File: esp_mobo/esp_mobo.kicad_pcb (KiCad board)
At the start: 2 copper layers, 75.5 x 107 mm, 4 parts, among them J1 JST XH Power in, U1 ESP32-DevKitC, U2 74AHCT125

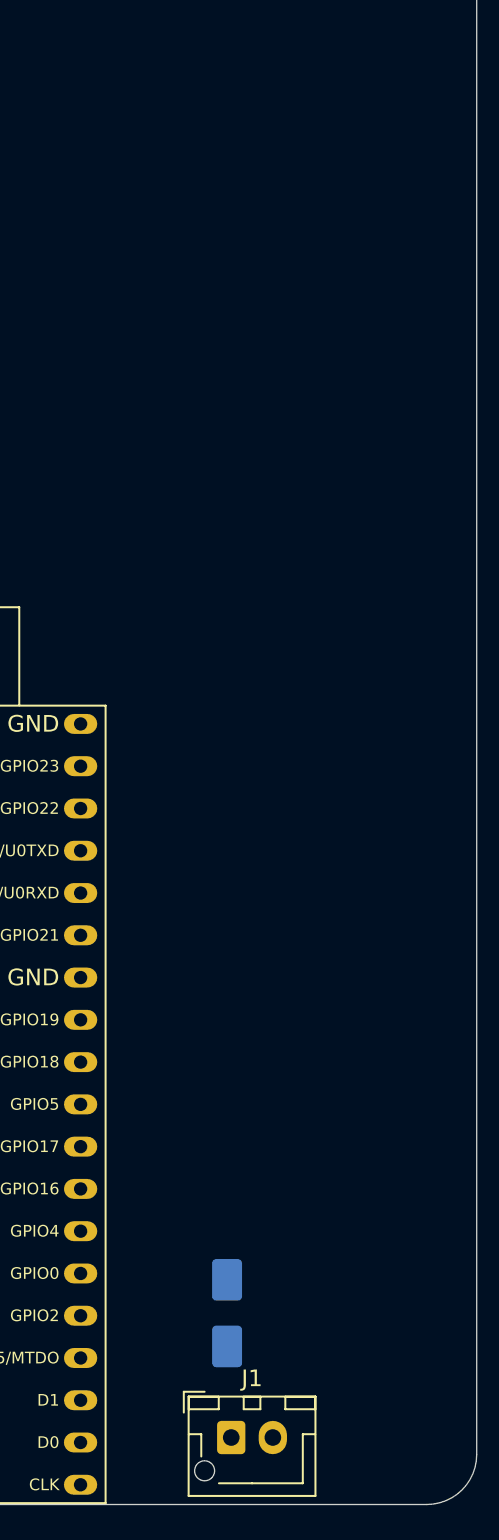
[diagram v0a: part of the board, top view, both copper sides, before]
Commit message: add submodule for testing
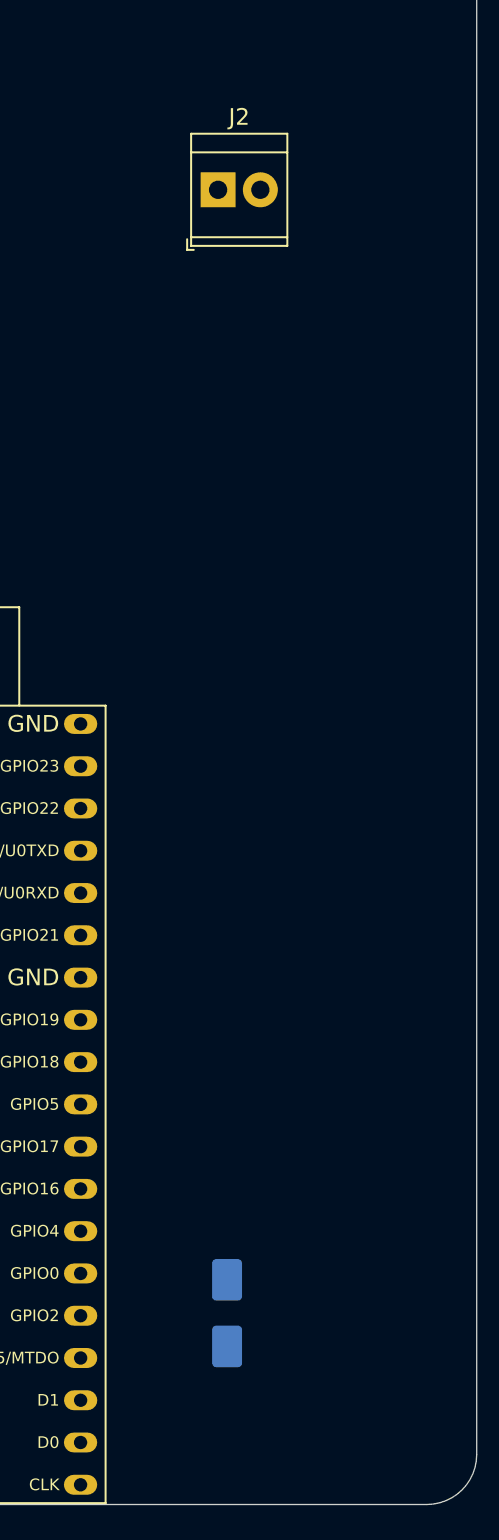
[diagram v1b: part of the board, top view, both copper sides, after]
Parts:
- removed J1: JST XH Power in, Connector_JST:JST_XH_B2B-XH-AM_1x02_P2.50mm_Vertical
- added J2: Screw_Terminal_01x02, TerminalBlock_TE-Connectivity:TerminalBlock_TE_282834-2_1x02_P2.54mm_Horizontal, F.Cu at (168.0, 62.5)
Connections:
- U1 pad 12: unconnected-(U1-MTMS/GPIO14/ADC2_CH6-Pad12) -> Motor 3 Signal
- U1 pad 13: unconnected-(U1-MTDI/GPIO12/ADC2_CH5-Pad13) -> Motor 1 Signal
- U1 pad 15: unconnected-(U1-MTCK/GPIO13/ADC2_CH4-Pad15) -> Motor 2 Signal
- U1 pad 23: unconnected-(U1-MTDO/GPIO15/ADC2_CH3-Pad23) -> Motor 4 Signal
- U1 pad 24: unconnected-(U1-ADC2_CH2/GPIO2-Pad24) -> Neopixel Data Out 3.3V
- U1 pad 27: unconnected-(U1-GPIO16-Pad27) -> Motor 5 Signal
- U1 pad 28: unconnected-(U1-GPIO17-Pad28) -> Motor 6 Signal
- U1 pad 30: unconnected-(U1-GPIO18-Pad30) -> Motor 7 Signal
- U1 pad 31: unconnected-(U1-GPIO19-Pad31) -> Motor 8 Signal
- U1 pad 34: unconnected-(U1-U0RXD/GPIO3-Pad34) -> RX
- U1 pad 35: unconnected-(U1-U0TXD/GPIO1-Pad35) -> TX
- U2 pad 1: unconnected-(U2-Pad1) -> GND
- U2 pad 10: unconnected-(U2-Pad10) -> GND
- U2 pad 13: unconnected-(U2-Pad13) -> GND
- U2 pad 14: unconnected-(U2E-VCC-Pad14) -> +5V
- U2 pad 2: unconnected-(U2-Pad2) -> Neopixel Data Out 3.3V
- U2 pad 3: unconnected-(U2-Pad3) -> Neopixel Data Out 5V
- U2 pad 4: unconnected-(U2-Pad4) -> GND
- U2 pad 7: unconnected-(U2E-GND-Pad7) -> GND

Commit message: Update ESC Mobo
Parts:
- added 5V: Conn_01x03_Pin, Connector_PinHeader_2.54mm:PinHeader_1x03_P2.54mm_Vertical, F.Cu at (115.1, 54.1)
- added F1: Polyfuse, Fuse:Fuse_Bourns_MF-RG300, F.Cu at (126.4, 56.5)
- added GND: Conn_01x03_Pin, Connector_PinHeader_2.54mm:PinHeader_1x03_P2.54mm_Vertical, F.Cu at (110.0, 54.1)
- added J1: Conn_01x04_Pin, Connector_JST:JST_XH_B4B-XH-AM_1x04_P2.50mm_Vertical, F.Cu at (152.9, 38.5)
- added J3: Conn_01x03_Pin, Connector_JST:JST_XH_B3B-XH-AM_1x03_P2.50mm_Vertical, F.Cu at (127.4, 38.5)
- added J4: Conn_01x03_Pin, Connector_JST:JST_XH_B3B-XH-AM_1x03_P2.50mm_Vertical, F.Cu at (138.9, 38.5)
- added R1: 220, Resistor_SMD:R_0805_2012Metric_Pad1.20x1.40mm_HandSolder, F.Cu at (125.0, 46.0)
- added R10: 220, Resistor_SMD:R_0603_1608Metric_Pad0.98x0.95mm_HandSolder, F.Cu at (144.8, 53.0)
- added R11: 220, Resistor_SMD:R_0603_1608Metric_Pad0.98x0.95mm_HandSolder, F.Cu at (144.8, 55.5)
- added R12: 220, Resistor_SMD:R_0603_1608Metric_Pad0.98x0.95mm_HandSolder, F.Cu at (116.5, 77.5)
- added R13: 220, Resistor_SMD:R_0603_1608Metric_Pad0.98x0.95mm_HandSolder, F.Cu at (116.5, 82.5)
- added R14: 220, Resistor_SMD:R_0603_1608Metric_Pad0.98x0.95mm_HandSolder, F.Cu at (149.2, 48.0)
- added R15: 220, Resistor_SMD:R_0603_1608Metric_Pad0.98x0.95mm_HandSolder, F.Cu at (149.2, 50.5)
- added R16: 220, Resistor_SMD:R_0603_1608Metric_Pad0.98x0.95mm_HandSolder, F.Cu at (149.2, 53.0)
- added R17: 220, Resistor_SMD:R_0603_1608Metric_Pad0.98x0.95mm_HandSolder, F.Cu at (149.2, 55.5)
- added R2: 220, Resistor_SMD:R_0603_1608Metric_Pad0.98x0.95mm_HandSolder, F.Cu at (140.5, 48.0)
- added R3: 220, Resistor_SMD:R_0603_1608Metric_Pad0.98x0.95mm_HandSolder, F.Cu at (140.5, 50.5)
- added R4: 220, Resistor_SMD:R_0603_1608Metric_Pad0.98x0.95mm_HandSolder, F.Cu at (159.0, 77.0)
- added R5: 220, Resistor_SMD:R_0603_1608Metric_Pad0.98x0.95mm_HandSolder, F.Cu at (159.0, 82.5)
- added R6: 220, Resistor_SMD:R_0603_1608Metric_Pad0.98x0.95mm_HandSolder, F.Cu at (175.0, 67.0)
- added R7: 220, Resistor_SMD:R_0603_1608Metric_Pad0.98x0.95mm_HandSolder, F.Cu at (175.0, 72.5)
- added R8: 220, Resistor_SMD:R_0603_1608Metric_Pad0.98x0.95mm_HandSolder, F.Cu at (144.8, 48.0)
- added R9: 220, Resistor_SMD:R_0603_1608Metric_Pad0.98x0.95mm_HandSolder, F.Cu at (144.8, 50.5)
- added Sig: Conn_01x03_Pin, Connector_PinHeader_2.54mm:PinHeader_1x03_P2.54mm_Vertical, F.Cu at (112.5, 54.1)
- added U3: PC847, Package_DIP:DIP-16_W7.62mm, F.Cu at (163.3, 67.1)
- added U4: PC847, Package_DIP:DIP-16_W7.62mm, F.Cu at (120.6, 67.1)
- D1: moved to F.Cu
- moved D1 82.6 mm to (172.0, 47.5)
- moved U2 48.0 mm to (141.9, 67.1)
- moved J2 24.0 mm to (169.2, 38.5)
- moved U1 1.25 mm to (133.1, 94.6)
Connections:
- D1 pad 2: Net-(D1-A) -> GND
- J2 pad 1: Net-(D1-A) -> Net-(J2-Pin_1)
- U1 pad 26: unconnected-(U1-ADC2_CH0/GPIO4-Pad26) -> Servo1 Data In
- U1 pad 7: unconnected-(U1-32K_XP/GPIO32/ADC1_CH4-Pad7) -> Servo2 Data In
- U1 pad 8: unconnected-(U1-32K_XN/GPIO33/ADC1_CH5-Pad8) -> Servo3 Data In
- U2 pad 11: unconnected-(U2-Pad11) -> Servo3 Data Out
- U2 pad 12: unconnected-(U2-Pad12) -> Servo3 Data In
- U2 pad 5: unconnected-(U2-Pad5) -> Servo1 Data In
- U2 pad 6: unconnected-(U2-Pad6) -> Servo1 Data Out
- U2 pad 8: unconnected-(U2-Pad8) -> Servo2 Data Out
- U2 pad 9: unconnected-(U2-Pad9) -> Servo2 Data In

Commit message: Update ESC Mobo
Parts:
- removed 5V, GND, Sig: Conn_01x03_Pin, Connector_PinHeader_2.54mm:PinHeader_1x03_P2.54mm_Vertical
- added C1: C_Polarized, Capacitor_THT:CP_Radial_D5.0mm_P2.00mm, F.Cu at (169.5, 55.0)
- added C2: 100uf, Capacitor_SMD:C_0603_1608Metric, F.Cu at (137.5, 51.5)
- added C3: 100uf, Capacitor_SMD:C_0603_1608Metric, F.Cu at (157.0, 51.5)
- added C4: 100uf, Capacitor_SMD:C_0603_1608Metric, F.Cu at (150.5, 51.5)
- added C5: 100uf, Capacitor_SMD:C_0603_1608Metric, F.Cu at (144.0, 51.5)
- added D2: WS2812B, LED_SMD:LED_WS2812B_PLCC4_5.0x5.0mm_P3.2mm, F.Cu at (134.8, 57.0)
- added D3: WS2812B, LED_SMD:LED_WS2812B_PLCC4_5.0x5.0mm_P3.2mm, F.Cu at (141.4, 57.0)
- added D4: WS2812B, LED_SMD:LED_WS2812B_PLCC4_5.0x5.0mm_P3.2mm, F.Cu at (148.0, 57.0)
- added D5: WS2812B, LED_SMD:LED_WS2812B_PLCC4_5.0x5.0mm_P3.2mm, F.Cu at (154.6, 57.0)
- added H1: MountingHole_Pad, MountingHole:MountingHole_3.2mm_M3_Pad, F.Cu at (178.0, 40.0)
- added H2: MountingHole_Pad, MountingHole:MountingHole_3.2mm_M3_Pad, F.Cu at (113.5, 40.0)
- added H3: MountingHole_Pad, MountingHole:MountingHole_3.2mm_M3_Pad, F.Cu at (113.5, 136.0)
- added H4: MountingHole_Pad, MountingHole:MountingHole_3.2mm_M3_Pad, F.Cu at (178.0, 136.0)
- added J10: Conn_01x03_Pin, Connector_PinHeader_2.54mm:PinHeader_1x03_P2.54mm_Vertical, F.Cu at (178.6, 101.5)
- added J11: Conn_01x03_Pin, Connector_PinHeader_2.54mm:PinHeader_1x03_P2.54mm_Vertical, F.Cu at (178.6, 105.0)
- added J12: Conn_01x03_Pin, Connector_PinHeader_2.54mm:PinHeader_1x03_P2.54mm_Vertical, F.Cu at (178.6, 108.5)
- added J13: Conn_01x03_Pin, Connector_PinHeader_2.54mm:PinHeader_1x03_P2.54mm_Vertical, F.Cu at (178.6, 115.0)
- added J14: Conn_01x03_Pin, Connector_PinHeader_2.54mm:PinHeader_1x03_P2.54mm_Vertical, F.Cu at (178.6, 122.8)
- added J15: Conn_01x03_Pin, Connector_PinHeader_2.54mm:PinHeader_1x03_P2.54mm_Vertical, F.Cu at (178.6, 112.0)
- added J16: Conn_01x02_Pin, Connector_PinHeader_2.54mm:PinHeader_1x02_P2.54mm_Vertical, F.Cu at (168.5, 110.0)
- added J5: Conn_01x03_Pin, Connector_PinHeader_2.54mm:PinHeader_1x03_P2.54mm_Vertical, F.Cu at (111.5, 51.5)
- added J6: Conn_01x03_Pin, Connector_PinHeader_2.54mm:PinHeader_1x03_P2.54mm_Vertical, F.Cu at (114.0, 51.5)
- added J7: Conn_01x03_Pin, Connector_PinHeader_2.54mm:PinHeader_1x03_P2.54mm_Vertical, F.Cu at (116.6, 51.5)
- added J8: Conn_01x03_Pin, Connector_PinHeader_2.54mm:PinHeader_1x03_P2.54mm_Vertical, F.Cu at (178.6, 95.0)
- added J9: Conn_01x03_Pin, Connector_PinHeader_2.54mm:PinHeader_1x03_P2.54mm_Vertical, F.Cu at (178.6, 98.0)
- moved R9 44.0 mm to (175.0, 82.5)
- moved F1 42.7 mm to (167.5, 45.0), turned to -90 degrees
- moved R8 41.9 mm to (175.0, 77.0)
- moved R11 32.6 mm to (117.0, 72.5)
- moved R17 31.8 mm to (132.5, 82.5), turned to 180 degrees
- moved R10 31.2 mm to (117.0, 67.0)
- moved R16 29.3 mm to (132.5, 77.0), turned to 180 degrees
- moved R3 29.1 mm to (160.0, 72.0)
- moved R2 27.3 mm to (160.0, 67.0)
- moved R15 27.3 mm to (132.5, 72.0), turned to 180 degrees
- moved R14 25.3 mm to (132.5, 67.0), turned to 180 degrees
- moved D1 2.00 mm to (174.0, 47.5), turned to 90 degrees
- moved R1 1.00 mm to (125.0, 45.0)
- moved R4 1.00 mm to (160.0, 77.0)
- moved R5 1.00 mm to (160.0, 82.5)
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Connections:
- U2 pad 3: Neopixel Data Out 5V -> NeoPixel Onboard
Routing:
- net GND: track 0.00 -> 166.8 mm, vias 0 -> 1
- net Motor 2 Signal: track 0.00 -> 115.1 mm
- net Motor 7 Signal: track 0.00 -> 109.5 mm
- net Motor 3 Signal: track 0.00 -> 109.4 mm
- net Motor 1 Signal: track 0.00 -> 106.4 mm
- net Motor 8 Signal: track 0.00 -> 94.9 mm
- net +5V: track 0.00 -> 91.9 mm
- net Neopixel Data Out 3.3V: track 0.00 -> 83.1 mm
- net Servo1 Data In: track 0.00 -> 76.8 mm
- net SDA: track 0.00 -> 72.1 mm
- net SCL: track 0.00 -> 69.1 mm
- net Motor 4 Signal: track 0.00 -> 63.0 mm
- net Servo2 Data Out: track 0.00 -> 57.4 mm, vias 0 -> 1
- net Servo1 Data Out: track 0.00 -> 54.9 mm
- net NeoPixel Onboard: track 0.00 -> 53.4 mm
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- added copper zone on F.Cu, net +5V
- added copper zone on B.Cu, net GND

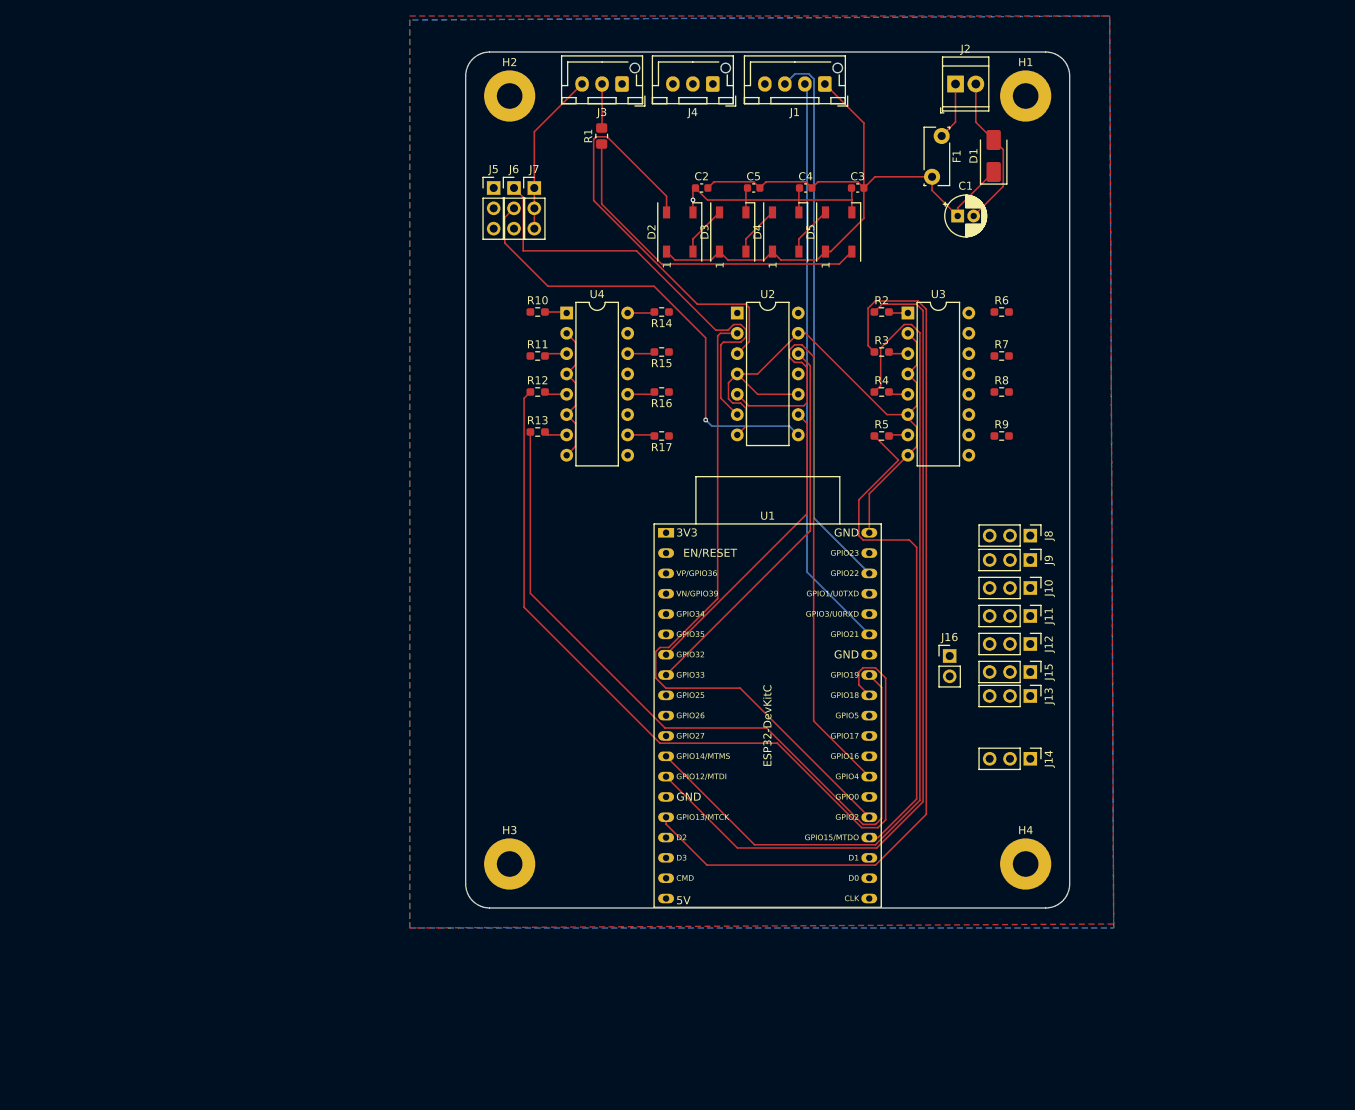
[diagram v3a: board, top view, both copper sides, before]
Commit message: Update ESC Mobo with BME280
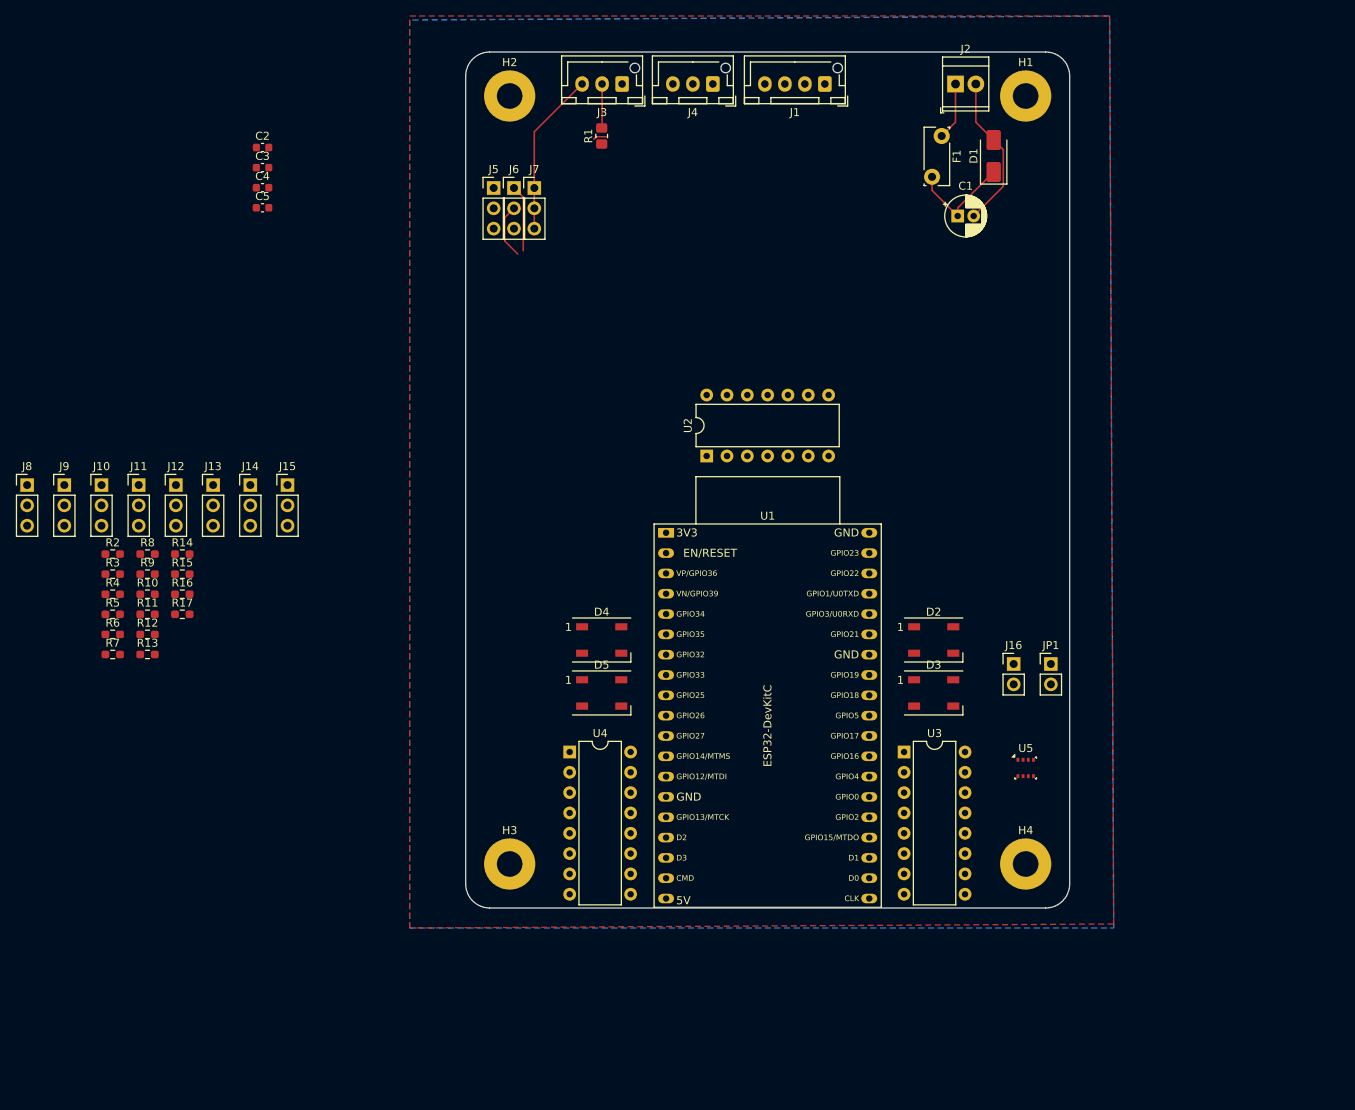
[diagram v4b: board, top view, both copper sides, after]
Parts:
- added JP1: Jumper_2_Open, Connector_PinHeader_2.54mm:PinHeader_1x02_P2.54mm_Vertical, F.Cu at (181.2, 111.0)
- added U5: BME280, Package_LGA:Bosch_LGA-8_2.5x2.5mm_P0.65mm_ClockwisePinNumbering, F.Cu at (178.0, 124.0)
- moved J8 125.6 mm to (53.2, 88.6), turned to 0 degrees
- moved J9 121.1 mm to (57.8, 88.6), turned to 0 degrees
- moved R6 118.2 mm to (63.9, 107.3)
- moved R7 117.2 mm to (63.9, 109.8)
- moved J10 116.8 mm to (62.5, 88.6), turned to 0 degrees
- moved J11 112.6 mm to (67.1, 88.6), turned to 0 degrees
- moved R8 108.7 mm to (68.2, 97.3)
- moved J12 108.6 mm to (71.8, 88.6), turned to 0 degrees
- moved R9 108.2 mm to (68.2, 99.8)
- moved J13 105.5 mm to (76.4, 88.6), turned to 0 degrees
- moved J14 103.3 mm to (81.1, 88.6), turned to 0 degrees
- moved R2 100.8 mm to (63.9, 97.3)
- moved R3 100.1 mm to (63.9, 99.8)
- moved R4 99.4 mm to (63.9, 102.3)
- moved R5 98.7 mm to (63.9, 104.8)
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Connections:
- U1 pad 1: unconnected-(U1-3V3-Pad1) -> +3.3V
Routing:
- net GND: track 166.8 -> 40.0 mm, vias 1 -> 0
- net Motor 2 Signal: track 115.1 -> 0.00 mm
- net Motor 7 Signal: track 109.5 -> 0.00 mm
- net Motor 3 Signal: track 109.4 -> 0.00 mm
- net Motor 1 Signal: track 106.4 -> 0.00 mm
- net Motor 8 Signal: track 94.9 -> 0.00 mm
- net Neopixel Data Out 3.3V: track 83.1 -> 0.00 mm
- net +5V: track 91.9 -> 13.6 mm
- net Servo1 Data In: track 76.8 -> 0.00 mm
- net SDA: track 72.1 -> 0.38 mm
- net SCL: track 69.1 -> 0.00 mm
- net Motor 4 Signal: track 63.0 -> 0.00 mm
- net NeoPixel Onboard: track 53.4 -> 1.82 mm
- net Servo2 Data Out: track 57.4 -> 6.86 mm, vias 1 -> 0
- net Servo3 Data In: track 48.3 -> 0.00 mm
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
